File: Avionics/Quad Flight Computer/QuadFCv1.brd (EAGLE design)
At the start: 76.2 x 50.5 mm, 3 parts, among them U1 LPC1769LQFP100

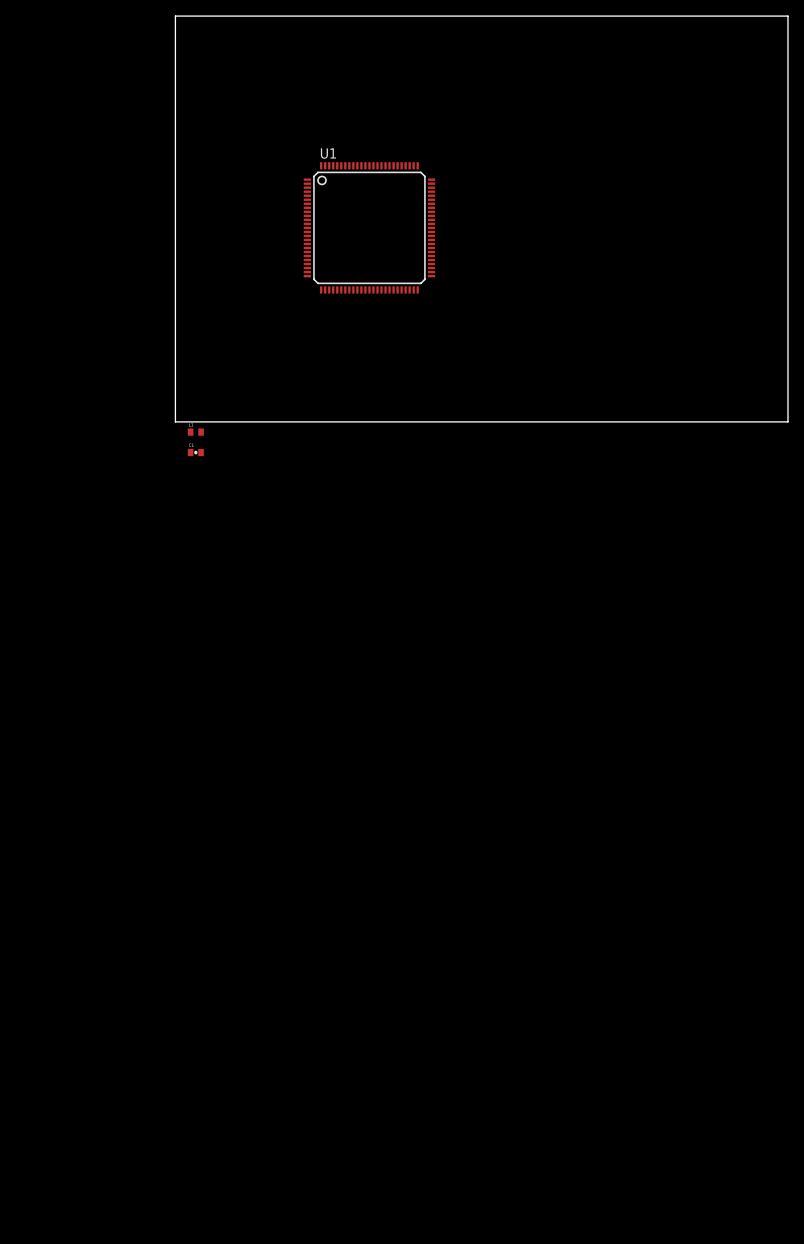
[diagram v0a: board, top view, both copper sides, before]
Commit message: Broke out all of the flight computer MCU ports and assigned the dedicated signals for use internally.
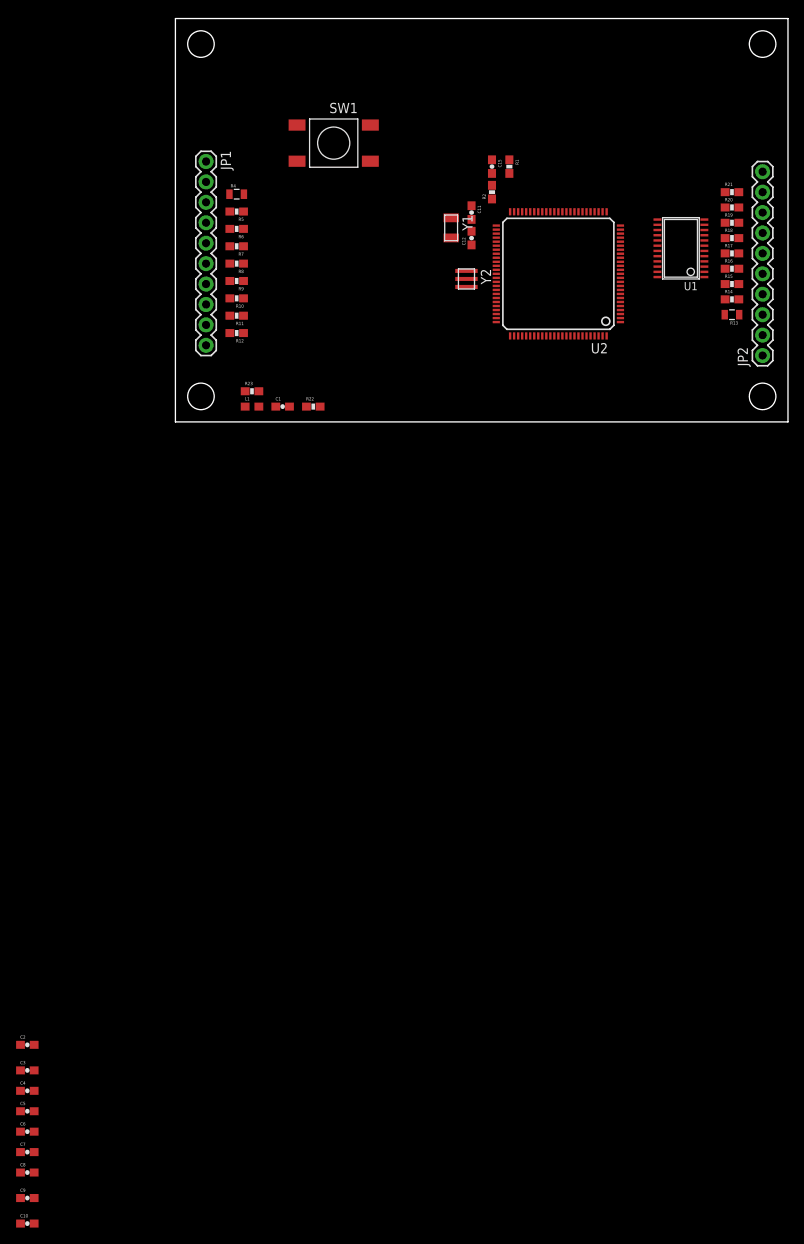
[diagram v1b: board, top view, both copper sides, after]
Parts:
- added C10, C15, C4, C5, C6, C7, C8, C9: 0.1uF, SparkFun-Capacitors:0603-CAP
- added C11, C12: 18pF, SparkFun-Capacitors:0603-CAP
- added C2: 3.3uF, SparkFun-Capacitors:0603-CAP
- added C3: 1uF, SparkFun-Capacitors:0603-CAP
- added JP1, JP2: M10", SparkFun-Connectors:1X10
- added R1, R2, R22: 10K, SparkFun-Resistors:0603-RES
- added R10, R11, R12, R14, R15, R16, R17, R18, R19, R20, R21, R5, R6, R7, R8, R9: 220, SparkFun-Resistors:0603-RES
- added R13, R4: 0, SparkFun-Resistors:0805
- added R23: 49.9K, SparkFun-Resistors:0603-RES
- added STANDOFF1, STANDOFF2, STANDOFF3, STANDOFF4: STAND-OFF, SparkFun-Electromechanical:STAND-OFF
- added SW1: 2-1437565-9, Shared Libraries:SMD_BUTTON_6X6
- added U2: TM4C123GH6PZ, Shared Libraries:LQFP100
- added Y1: 32.768KHZ, Shared Libraries:ECS-.327-12.5-34B
- added Y2: AWSCR-20.00CW-T, Shared Libraries:AWSCR-CW
- C1: device SparkFun-Passives:0402-CAP -> SparkFun-Passives:0603-CAP
- L1: device SparkFun-Passives:C0402 -> SparkFun-Passives:0603
- U1: value LPC1769LQFP100 -> 74LVC4245APW; device Shared Libraries:LQFP100 -> Shared Libraries:TSSOP24
- moved U1 38.8 mm to (62.9, 21.6), turned to 90 degrees
- moved C1 12.2 mm to (13.3, 1.91)
- moved L1 7.67 mm to (9.53, 1.91)
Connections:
- new net 5V: R13.2, R4.2, U1.1
- new net FC_AIN0: U2.12
- new net FC_AIN1: U2.13
- new net FC_AIN20: U2.90
- new net FC_AIN21: U2.89
- new net FC_AIN4: U2.100
- new net FC_AIN5: U2.99
- new net FC_I2C3SCL: U2.62
- new net FC_I2C3SDA: U2.61
- new net FC_JTAG_TCK: U2.85
- new net FC_JTAG_TDI: U2.83
- new net FC_JTAG_TDO: U2.82
- new net FC_JTAG_TMS: U2.84
- new net FC_PA6: U2.34
- new net FC_PA7: U2.35
- new net FC_PB2: U2.72
- new net FC_PB3: U2.73
- new net FC_PB4: U2.92
- new net FC_PB5: U2.91
- new net FC_PD0: U2.1
- new net FC_PD1: U2.2
- new net FC_PD2: U2.3
- new net FC_PD3: U2.4
- new net FC_PD4: U2.97
- new net FC_PD5: U2.98
- new net FC_PE4: U2.95
- new net FC_PE5: U2.96
- new net FC_PF0: U2.40
- new net FC_PF1: U2.41
- new net FC_PF2: U2.42
- new net FC_PF3: U2.43
- new net FC_PF4: U2.39
- new net FC_PF5: U2.37
- new net FC_PF6: U2.36
- new net FC_PF7: U2.58
- new net FC_PG2: U2.60
- new net FC_PG3: U2.59
- new net FC_PG4: U2.74
- new net FC_PG5: U2.75
- new net FC_PG6: U2.87
- new net FC_PG7: U2.88
- new net FC_PJ2: U2.11
- new net FC_PWMOUT1: U1.21, U2.16
- new net FC_PWMOUT2: U1.20, U2.17
- new net FC_PWMOUT3: U1.19, U2.18
- new net FC_PWMOUT4: U1.18, U2.19
- new net FC_PWMOUT5: U1.17, U2.79
- new net FC_PWMOUT6: U1.16, U2.78
- new net FC_PWMOUT7: U1.15, U2.77
- new net FC_PWMOUT8: U1.14, U2.76
- new net FC_PWMOUT_ARM_L: R23.1, U1.22
- new net FC_RESET_L: C15.1, R1.1, SW1.1, SW1.2, U2.63
- new net FC_SSI0CLK: U2.28
- new net FC_SSI0FSS: U2.29
- new net FC_SSI0RX: U2.30
- new net FC_SSI0TX: U2.31
- new net FC_SSI3CLK: U2.49
- new net FC_SSI3FSS: U2.48
- new net FC_SSI3RX: U2.47
- new net FC_SSI3TX: U2.46
- new net FC_U0RX: U2.26
- new net FC_U0TX: U2.27
- new net FC_U1RX: U2.25
- new net FC_U1TX: U2.24
- new net FC_U3RX: U2.23
- new net FC_U3TX: U2.22
- new net FC_U7RX: U2.15
- new net FC_U7TX: U2.14
- new net FC_USB0DM: U2.68
- new net FC_USB0DP: U2.69
- new net FC_USB0ID: U2.70
- new net FC_USB0VBUS: U2.71
- new net GNDX: C11.2, C12.2, U2.53
- new net N$10: JP2.4, R15.2
- new net N$11: JP2.5, R16.2
- new net N$12: JP2.6, R17.2
- new net N$13: JP2.7, R18.2
- new net N$14: JP2.8, R19.2
- new net N$15: JP2.9, R20.2
- new net N$16: JP2.10, R21.2
- new net N$17: C1.2, L1.1, U2.8
- new net N$18: C2.1, U2.38, U2.86
- new net N$19: C12.1, U2.54, Y1.P$2
- new net N$2: JP1.4, R6.2
- new net N$20: R22.2, U1.2
- new net N$21: C11.1, U2.52, Y1.P$1
- new net N$22: R2.1, U2.50
- new net N$23: JP1.2, R4.1
- new net N$24: U2.65, Y2.P$1
- new net N$25: U2.66, Y2.P$3
- new net N$26: JP2.2, R13.1
- new net N$3: JP1.5, R7.2
- new net N$4: JP1.6, R8.2
- new net N$5: JP1.7, R9.2
- new net N$6: JP1.8, R10.2
- new net N$7: JP1.9, R11.2
- new net N$8: JP1.10, R12.2
- new net N$9: JP2.3, R14.2
- new net PWMIN1: R5.1
- new net PWMIN2: R6.1
- new net PWMIN3: R7.1
- new net PWMIN4: R8.1
- new net PWMIN5: R9.1
- new net PWMIN6: R10.1
- new net PWMIN7: R11.1
- new net PWMIN8: R12.1
- new net PWMOUT1: R14.1, U1.3
- new net PWMOUT2: R15.1, U1.4
- new net PWMOUT3: R16.1, U1.5
- new net PWMOUT4: R17.1, U1.6
- new net PWMOUT5: R18.1, U1.7
- new net PWMOUT6: R19.1, U1.8
- new net PWMOUT7: R20.1, U1.9
- new net PWMOUT8: R21.1, U1.10
- net 3.3V: now also C10.1, C3.1, C4.1, C5.1, C6.1, C7.1, C8.1, C9.1, L1.2, R1.2, R23.2, U1.23, U1.24, U2.20, U2.32, U2.44, U2.5, U2.55, U2.56, U2.67, U2.7, U2.80, U2.93; no longer L1.1, U1.19, U1.28, U1.42, U1.54, U1.71, U1.84, U1.96
- net GND: now also C1.1, C10.2, C15.2, C2.2, C3.2, C4.2, C5.2, C6.2, C7.2, C8.2, C9.2, JP1.1, JP2.1, R2.2, R22.1, SW1.3, SW1.4, U1.12, U1.13, U2.10, U2.21, U2.33, U2.45, U2.57, U2.6, U2.64, U2.81, U2.9, U2.94, Y2.P$2; no longer C1.2, U1.15, U1.31, U1.41, U1.55, U1.72, U1.83, U1.97
- net N$1: now also JP1.3, R5.2; no longer C1.1, L1.2, U1.10, U1.12
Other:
- board size 76.2 x 50.5 mm -> 76.2 x 50.2 mm

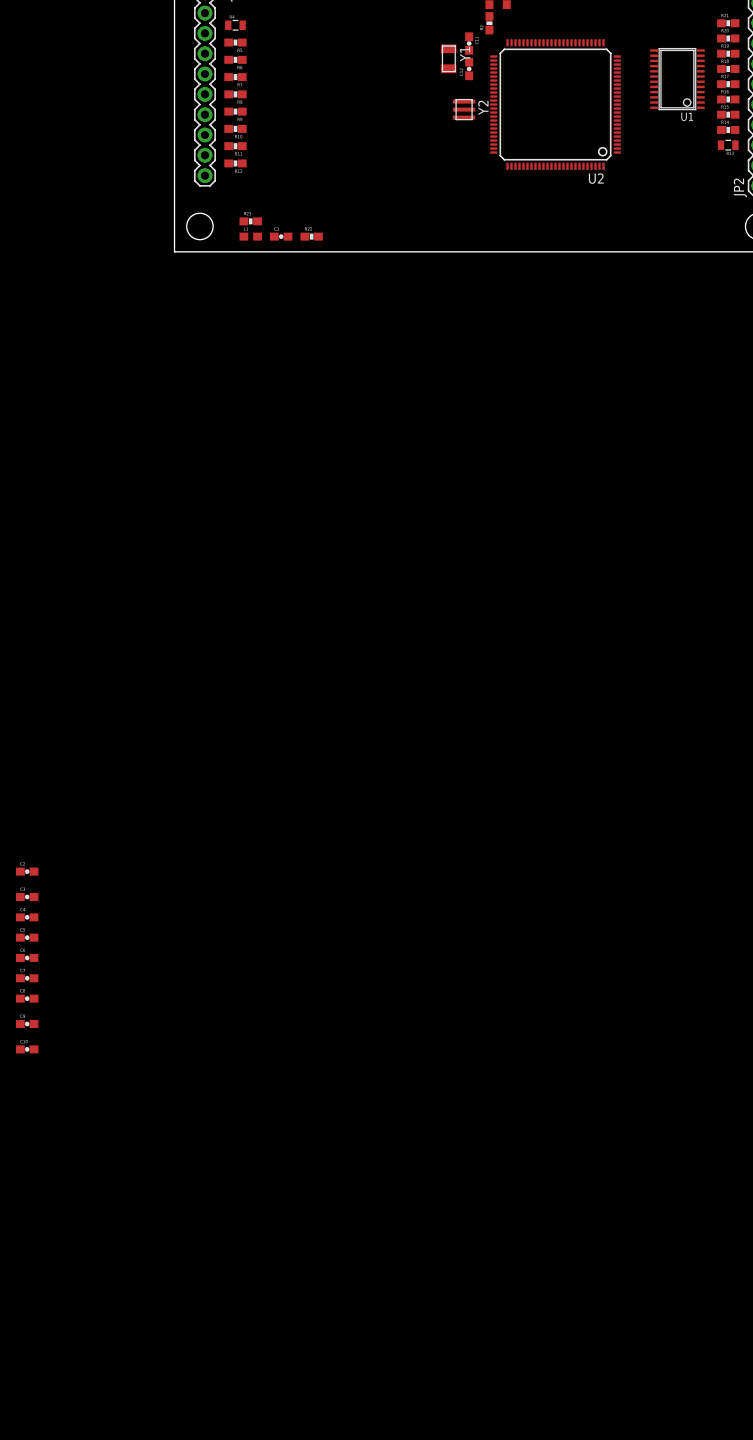
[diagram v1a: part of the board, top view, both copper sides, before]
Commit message: Added PPM encoder framework from Ardupilot mega schematic
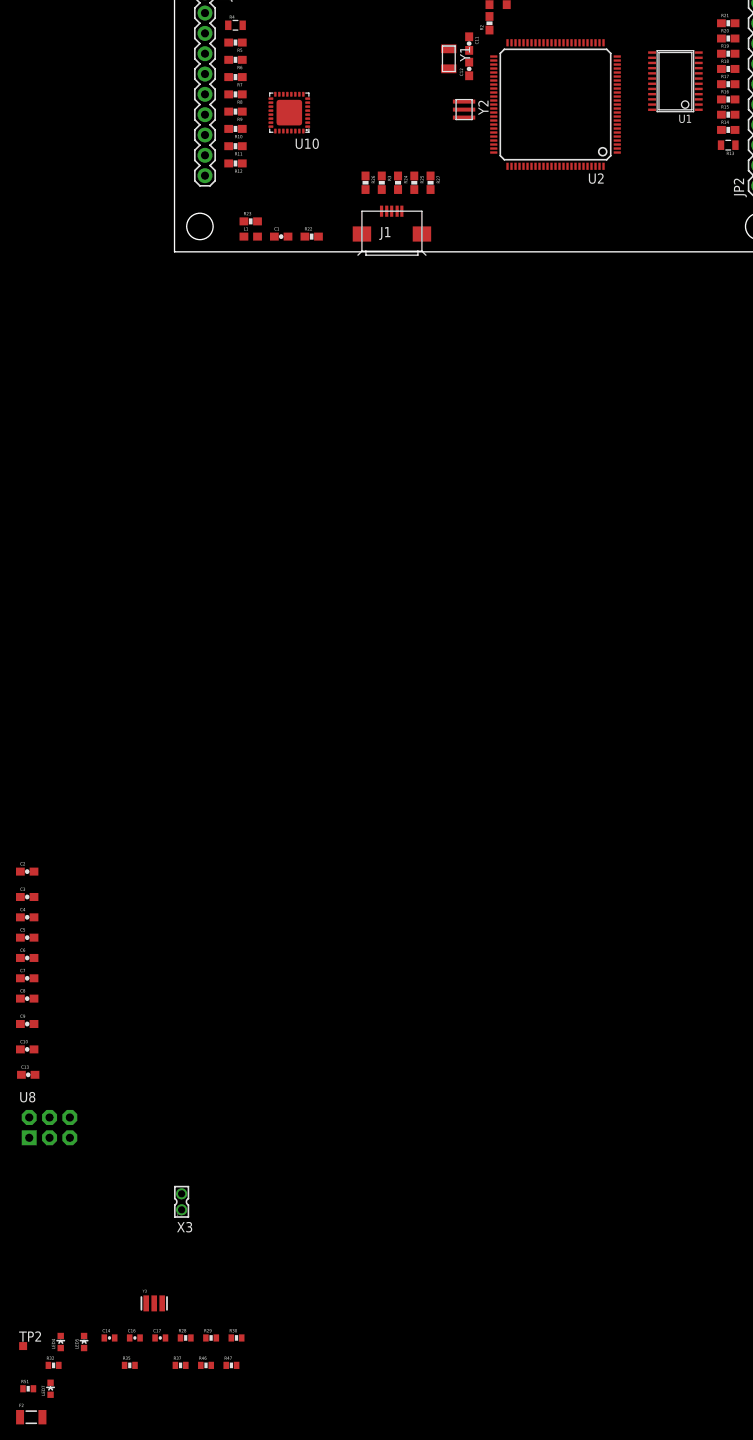
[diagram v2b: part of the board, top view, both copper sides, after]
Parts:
- added C13: 1uF, SparkFun-Capacitors:0603-CAP
- added C14, C16: .1uF, SparkFun:0402-CAP
- added C17: 1uF, SparkFun:0402-CAP
- added F2: 500mA, SparkFun:PTC-1206
- added J1: 10104111_MICROUSBAB, Shared Libraries:USB-AB-10104111
- added LED4, LED5: ORANGE, SparkFun:LED-0603
- added LED7: RED, SparkFun:LED-0603
- added R24, R3: 22, Shared Libraries:0603-RES
- added R25, R26: 22-DNP, Shared Libraries:0603-RES
- added R27: 0, Shared Libraries:0603-RES
- added R28: 1K, SparkFun:0402-RES
- added R29: 1M, SparkFun:0402-RES
- added R30: 27, SparkFun:0402-RES
- added R32, R35, R46, R47, R51: 1k, SparkFun:0402-RES
- added R37: 10K, SparkFun:0402-RES
- added TP2: TPSQTP10SQ, testpad:TP10SQ
- added U10: ATMEGA32U2-MU, atmel:QFN32
- added U8: SPI_PPM, SparkFunv2:2X3-NS
- added X3: HWB, con-molex:87758-0216
- added Y3: 16MHz, SmartPrj:RESONATOR
- C2: value 3.3uF -> 1uF
- moved U1 0.36 mm to (62.6, 21.3)
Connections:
- new net N$27: J1.4, R27.2
- new net N$28: J1.2, R26.2, R3.2
- new net N$29: J1.3, R24.2, R25.2
- new net N$30: LED5.A, R35.2
- new net N$31: LED4.A, R32.2
- new net N$32: LED7.A, R51.2
- new net PC7_LED: LED7.C, U10.22
- new net PPM_HWB: U10.13, X3.1
- new net PPM_OUT: R28.2, TP2.TP, U10.23
- new net PPM_PD0: R47.2, U10.6
- new net PPM_PD1: R46.2, U10.7
- new net PPM_RST: R37.1, U10.24, U8.5
- new net PPM_RX: U10.8
- new net PPM_TX: U10.9
- new net PPM_USBDM: R26.1, U10.30
- new net PPM_USBDP: R25.1, U10.29
- new net PPM_VBUS: U10.31
- new net RXLED: LED4.C, U10.10
- new net TXLED: LED5.C, U10.11
- new net VUCAP: C17.1, U10.27
- new net VUSB: J1.1
- new net XT1: R29.2, R30.1, Y3.3
- new net XT1R: R30.2, U10.1
- new net XT2: R29.1, U10.2, Y3.1
- net 5V: now also C14.1, C16.1, R32.1, R35.1, R37.2, R51.1, U10.32, U10.4, U8.2
- net FC_USB0DM: now also R3.1
- net FC_USB0DP: now also R24.1
- net FC_USB0ID: now also R27.1
- net GND: now also C13.2, C14.2, C16.2, C17.2, J1.5, J1.GND@1, J1.GND@2, U10.28, U10.3, U10.EXP, U8.6, X3.2, Y3.2
- net N$18: now also C13.1
- net PWMIN1: now also U10.14
- net PWMIN2: now also U10.15, U8.3
- net PWMIN3: now also U10.16, U8.4
- net PWMIN4: now also U10.17, U8.1
- net PWMIN5: now also U10.18
- net PWMIN6: now also U10.19
- net PWMIN7: now also U10.20
- net PWMIN8: now also U10.21

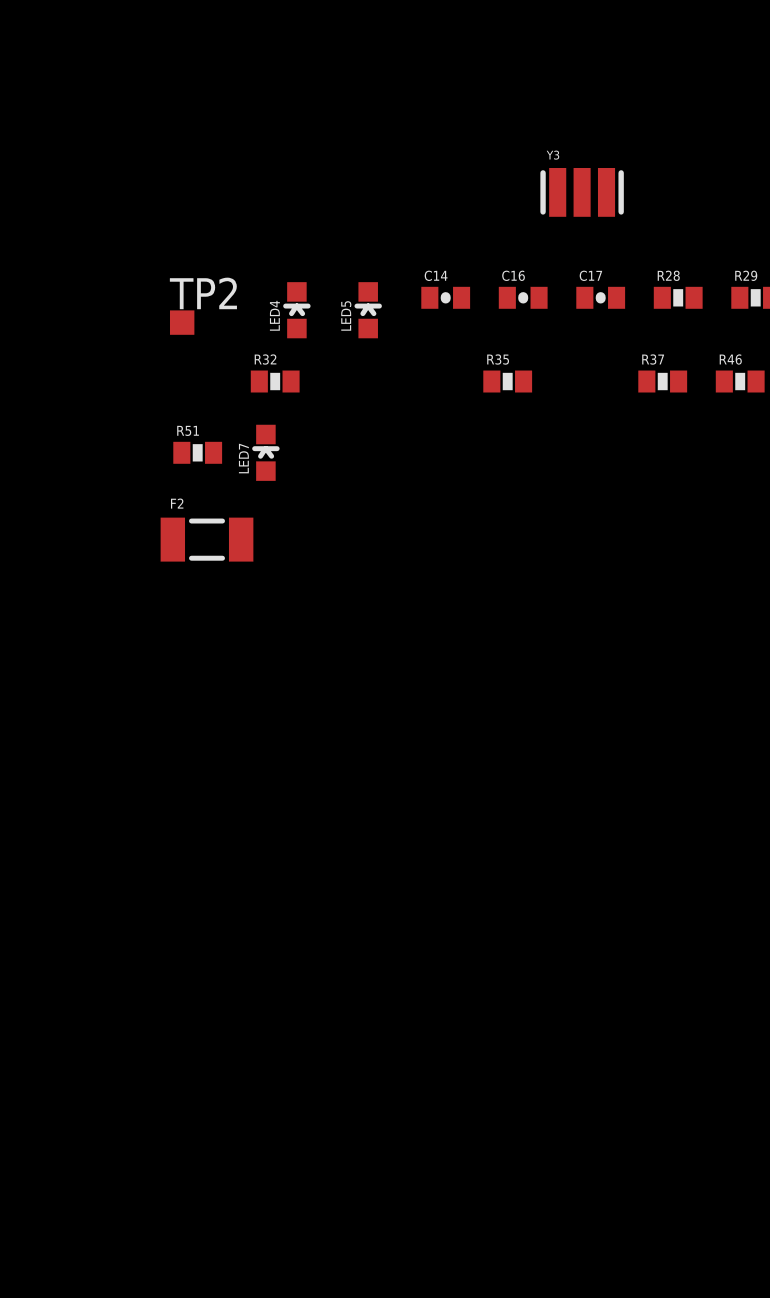
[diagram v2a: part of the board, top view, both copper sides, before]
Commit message: Added IMU. Needs some work
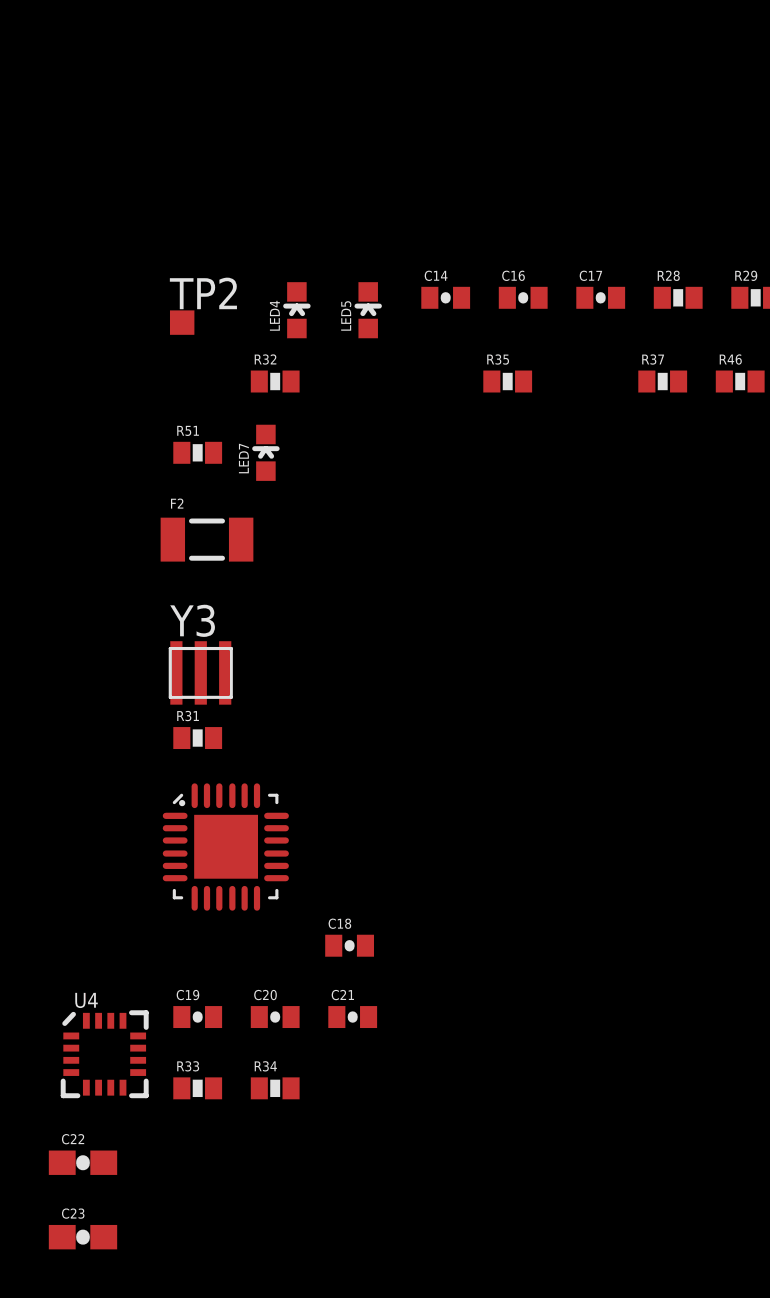
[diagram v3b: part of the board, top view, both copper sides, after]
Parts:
- added C18, C20: 0.1uF, SparkFun:0402-CAP
- added C19: 2.2nF, SparkFun:0402-CAP
- added C21: 10nF, SparkFun:0402-CAP
- added C22: 0.22uF, SparkFun-Capacitors:0603-CAP
- added C23: 4.7uF, SparkFun-Capacitors:0603-CAP
- added R31: 1k, SparkFun:0402-RES
- added R33, R34: 10k, SparkFun:0402-RES
- added U3: MPU-6050-1, Testing:QFN-24-4MM2
- added U4: HMC5883LSMD, Shared Libraries:16LPCC
- LED5: value ORANGE -> RED
- LED7: value RED -> GREEN
- Y3: value 16MHz -> PRQC16.00SR5010X000; device SmartPrj:RESONATOR -> Shared Libraries:PRQC16.00SR5010X000
- moved Y3 25.1 mm to (-18.2, -151.1)
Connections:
- removed net FC_I2C3SCL: U2.62
- removed net FC_I2C3SDA: U2.61
- new net AUX_SCL: U3.7
- new net AUX_SDA: U3.6
- new net FC_IMU_SCL: R33.1, U2.62, U3.23, U4.1
- new net FC_IMU_SDA: R34.1, U2.61, U3.24, U4.16
- new net FC_MAG_DRDY_L: U4.15
- new net IMU_INT: U3.12
- new net N$33: C19.1, U3.20
- new net N$34: C18.1, U3.10
- new net N$35: C23.1, U4.10
- new net N$36: C22.1, U4.8
- new net N$37: C22.2, U4.12
- new net PPM_STATUS0: R47.1
- new net PPM_STATUS1: R46.1
- new net PPM_USB_STATUS: R31.2, U10.5
- new net VIO: C21.1, U3.8
- net 3.3V: now also C20.1, R33.2, R34.2, U3.13, U4.13, U4.2, U4.4
- net GND: now also C18.2, C19.2, C20.2, C21.2, C23.2, U3.1, U3.11, U3.18, U3.9, U4.11, U4.9
